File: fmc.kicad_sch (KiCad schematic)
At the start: 2 parts, among them P1 ASP-134604-01, P2 ASP-134604-01

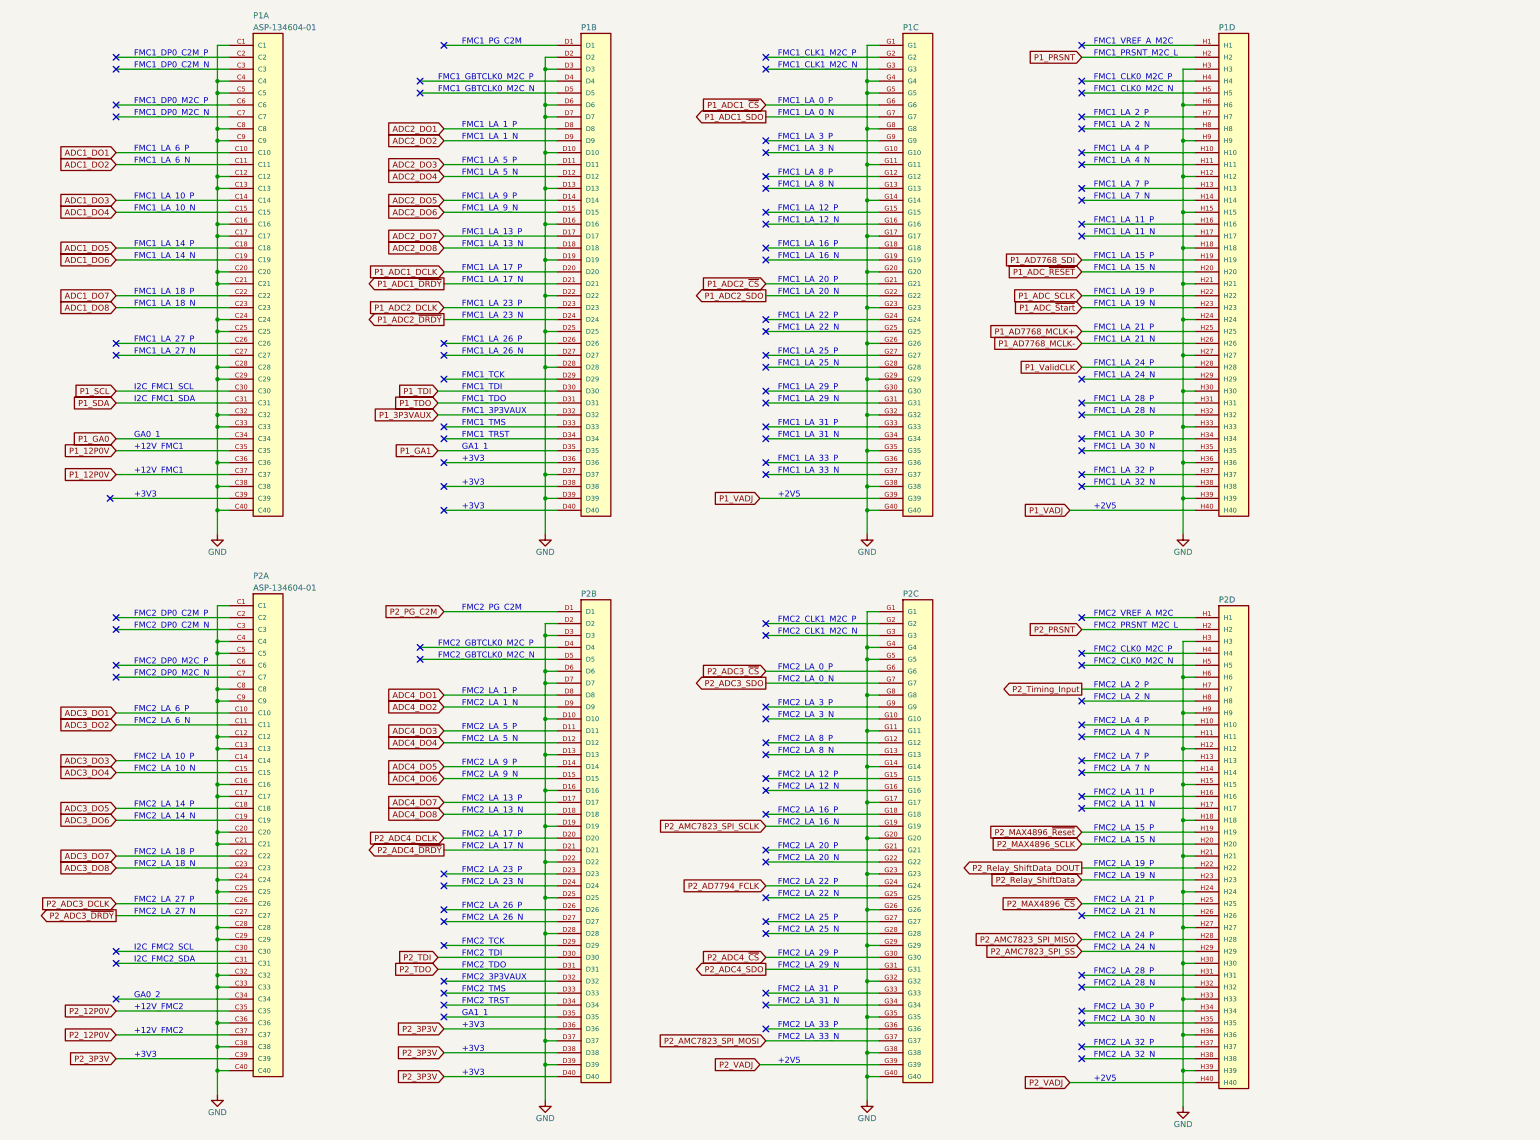
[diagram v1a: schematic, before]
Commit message: Update to Schematics; initial PCB commit
-Updated Power, Housekeeping, and ADCs sheets.
-Remapped FMC pins
-Initial board layout commit
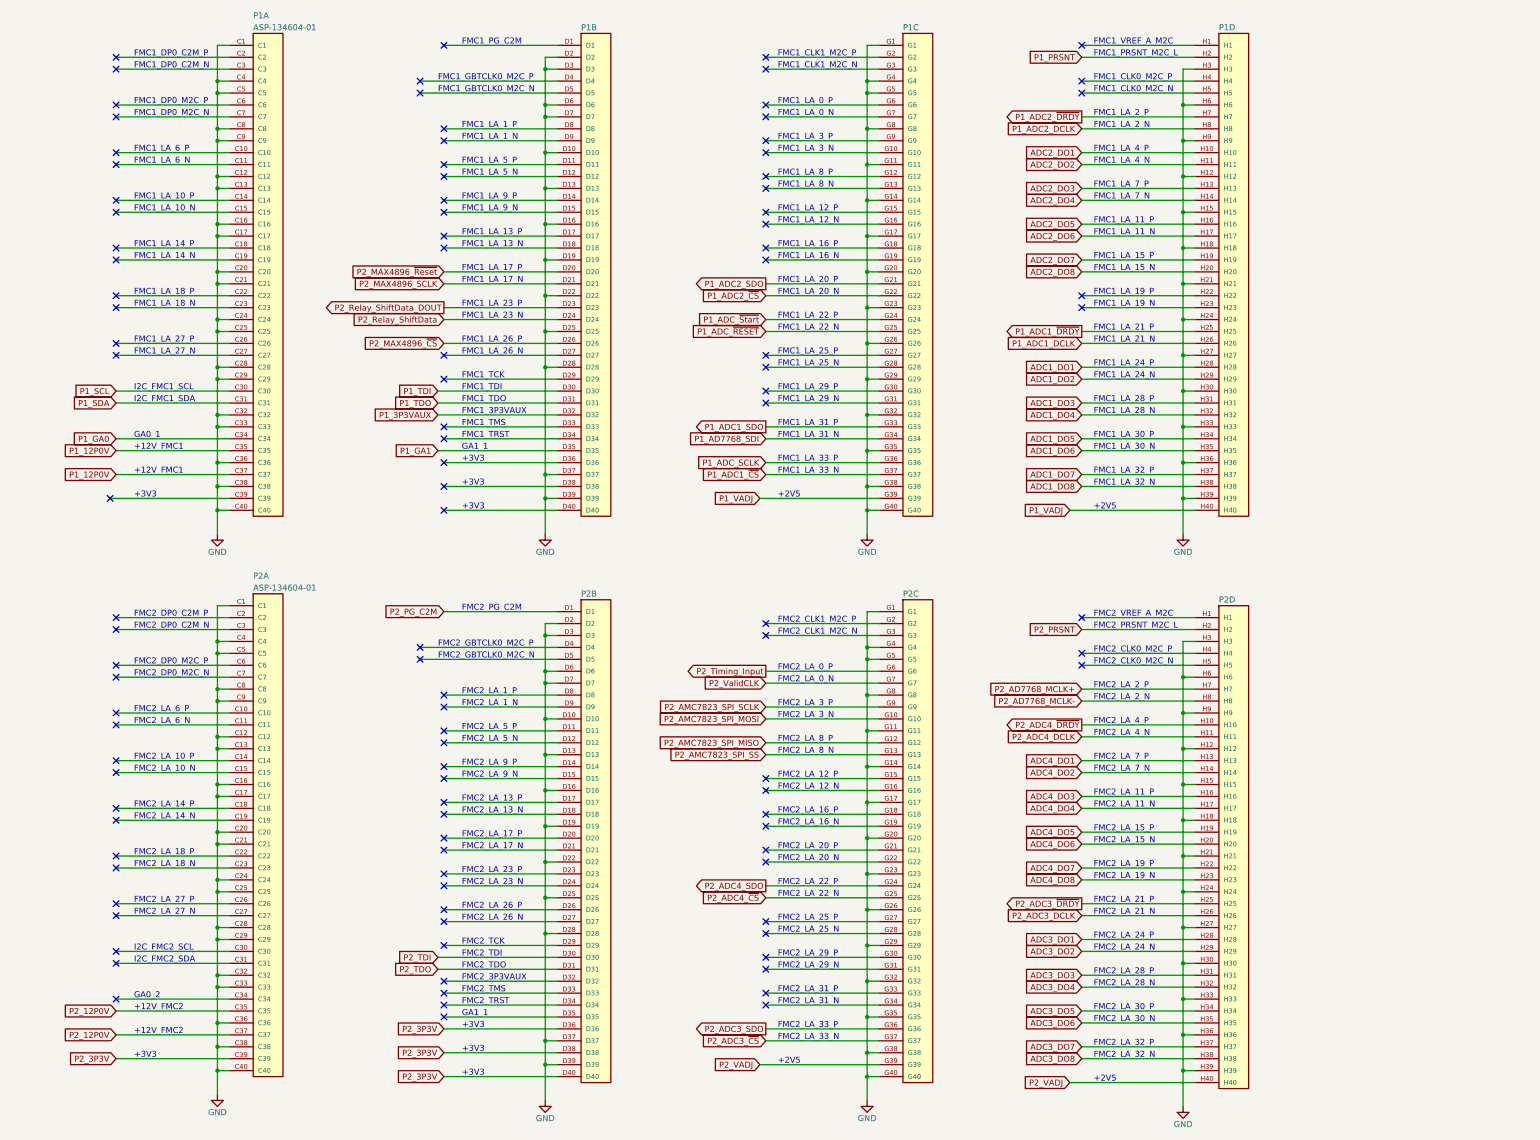
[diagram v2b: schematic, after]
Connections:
- net P1_AD7768_MCLK+ is gone; now on net P1_ADC1_~{DRDY}: P1.H25
- net P1_AD7768_MCLK- is gone; now on net P1_ADC1_DCLK: P1.H26
- net P1_ValidCLK is gone; now on net ADC1_DO1: P1.H28
- net P2_AD7794_FCLK is gone; now on net P2_ADC4_SDO: P2.G24
- net ADC1_DO1: no longer P1.C10
- net ADC1_DO2: now also P1.H29; no longer P1.C11
- net ADC1_DO3: now also P1.H31; no longer P1.C14
- net ADC1_DO4: now also P1.H32; no longer P1.C15
- net ADC1_DO5: now also P1.H34; no longer P1.C18
- net ADC1_DO6: now also P1.H35; no longer P1.C19
- net ADC1_DO7: now also P1.H37; no longer P1.C22
- net ADC1_DO8: now also P1.H38; no longer P1.C23
- net ADC2_DO1: now also P1.H10; no longer P1.D8
- net ADC2_DO2: now also P1.H11; no longer P1.D9
- net ADC2_DO3: now also P1.H13; no longer P1.D11
- net ADC2_DO4: now also P1.H14; no longer P1.D12
- net ADC2_DO5: now also P1.H16; no longer P1.D14
- net ADC2_DO6: now also P1.H17; no longer P1.D15
- net ADC2_DO7: now also P1.H19; no longer P1.D17
- net ADC2_DO8: now also P1.H20; no longer P1.D18
- net ADC3_DO1: now also P2.H28; no longer P2.C10
- net ADC3_DO2: now also P2.H29; no longer P2.C11
- net ADC3_DO3: now also P2.H31; no longer P2.C14
- net ADC3_DO4: now also P2.H32; no longer P2.C15
- net ADC3_DO5: now also P2.H34; no longer P2.C18
- net ADC3_DO6: now also P2.H35; no longer P2.C19
- net ADC3_DO7: now also P2.H37; no longer P2.C22
- net ADC3_DO8: now also P2.H38; no longer P2.C23
- net ADC4_DO1: now also P2.H13; no longer P2.D8
- net ADC4_DO2: now also P2.H14; no longer P2.D9
- net ADC4_DO3: now also P2.H16; no longer P2.D11
- net ADC4_DO4: now also P2.H17; no longer P2.D12
- net ADC4_DO5: now also P2.H19; no longer P2.D14
- net ADC4_DO6: now also P2.H20; no longer P2.D15
- net ADC4_DO7: now also P2.H22; no longer P2.D17
- net ADC4_DO8: now also P2.H23; no longer P2.D18
- net P1_AD7768_SDI: now also P1.G34; no longer P1.H19
- net P1_ADC1_DCLK: no longer P1.D20
- net P1_ADC1_SDO: now also P1.G33; no longer P1.G7
- net P1_ADC1_~{CS}: now also P1.G37; no longer P1.G6
- net P1_ADC1_~{DRDY}: no longer P1.D21
- net P1_ADC2_DCLK: now also P1.H8; no longer P1.D23
- net P1_ADC2_SDO: now also P1.G21; no longer P1.G22
- net P1_ADC2_~{CS}: now also P1.G22; no longer P1.G21
- net P1_ADC2_~{DRDY}: now also P1.H7; no longer P1.D24
- net P1_ADC_SCLK: now also P1.G36; no longer P1.H22
- net P1_ADC_~{RESET}: now also P1.G25; no longer P1.H20
- net P1_ADC_~{Start}: now also P1.G24; no longer P1.H23
- net P2_ADC3_DCLK: now also P2.H26; no longer P2.C26
- net P2_ADC3_SDO: now also P2.G36; no longer P2.G7
- net P2_ADC3_~{CS}: now also P2.G37; no longer P2.G6
- net P2_ADC3_~{DRDY}: now also P2.H25; no longer P2.C27
- net P2_ADC4_DCLK: now also P2.H11; no longer P2.D20
- net P2_ADC4_SDO: no longer P2.G31
- net P2_ADC4_~{CS}: now also P2.G25; no longer P2.G30
- net P2_ADC4_~{DRDY}: now also P2.H10; no longer P2.D21
- net P2_AMC7823_SPI_MISO: now also P2.G12; no longer P2.H28
- net P2_AMC7823_SPI_MOSI: now also P2.G10; no longer P2.G37
- net P2_AMC7823_SPI_SCLK: now also P2.G9; no longer P2.G19
- net P2_AMC7823_SPI_SS: now also P2.G13; no longer P2.H29
- net P2_MAX4896_SCLK: now also P1.D21; no longer P2.H20
- net P2_MAX4896_~{CS}: now also P1.D26; no longer P2.H25
- net P2_MAX4896_~{Reset}: now also P1.D20; no longer P2.H19
- net P2_Relay_ShiftData: now also P1.D24; no longer P2.H23
- net P2_Relay_ShiftData_DOUT: now also P1.D23; no longer P2.H22
- net P2_Timing_Input: now also P2.G6; no longer P2.H7
- net P2_AD7768_MCLK-: now reaches P2.H8
- new net P2_AD7768_MCLK+: P2.H7
- new net P2_ValidCLK: P2.G7
- no-connect marks 108 -> 109

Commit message: Updated Layout
-Additional Layout Work
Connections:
- net P1_ADC1_DCLK: now also P1.G33; no longer P1.H26
- net P1_ADC1_SDO: no longer P1.G33
- net P1_ADC1_~{DRDY}: no longer P1.H25
- net P1_ADC2_DCLK: now also P1.G27; no longer P1.H8
- net P1_ADC2_SDO: no longer P1.G21
- net P1_ADC2_~{CS}: now also P1.G28; no longer P1.G22
- net P1_ADC2_~{DRDY}: no longer P1.H7
- net P1_ADC_~{RESET}: now also P1.G31; no longer P1.G25
- net P1_ADC_~{Start}: now also P1.G30; no longer P1.G24
- net P2_MAX4896_~{Flag}: now reaches P2.D8
- no-connect marks 109 -> 104
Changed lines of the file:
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@@
   (no_connect (at 87.63 57.15))
   (no_connect (at 157.48 120.65))
-  (no_connect (at 157.48 160.02))
   (no_connect (at 226.06 147.32))
   (no_connect (at 87.63 34.29))
@@
   (no_connect (at 226.06 218.44))
   (no_connect (at 226.06 44.45))
-  (no_connect (at 226.06 87.63))
   (no_connect (at 226.06 67.31))
   (no_connect (at 293.37 74.93))
@@
   (no_connect (at 87.63 163.83))
   (no_connect (at 157.48 115.57))
-  (no_connect (at 226.06 95.25))
   (no_connect (at 157.48 64.77))
   (no_connect (at 157.48 162.56))
@@
   (no_connect (at 157.48 205.74))
   (no_connect (at 157.48 198.12))
-  (no_connect (at 226.06 90.17))
   (no_connect (at 157.48 223.52))
   (no_connect (at 157.48 105.41))
@@
   (no_connect (at 87.63 217.17))
   (no_connect (at 157.48 182.88))
-  (no_connect (at 226.06 97.79))
   (no_connect (at 157.48 208.28))
   (no_connect (at 226.06 215.9))
@@
     )
   )
-  (global_label "P1_ADC2_DCLK" (shape input) (at 293.37 39.37 180) (fields_autoplaced)
-    (effects (font (size 1.27 1.27)) (justify right))
-    (property "Intersheetrefs" "${INTERSHEET_REFS}" (at 276.2939 39.37 0)
-      (effects (font (size 1.27 1.27)) (justify right) hide)
-    )
-  )
   (global_label "P1_GA1" (shape input) (at 156.21 107.95 180) (fields_autoplaced)
     (effects (font (size 1.27 1.27)) (justify right))
@@
     )
   )
-  (global_label "P1_ADC2_SDO" (shape output) (at 226.06 72.39 180) (fields_autoplaced)
-    (effects (font (size 1.27 1.27)) (justify right))
-    (property "Intersheetrefs" "${INTERSHEET_REFS}" (at 210.012 72.39 0)
-      (effects (font (size 1.27 1.27)) (justify right) hide)
-    )
-  )
   (global_label "ADC3_DO6" (shape input) (at 293.37 229.87 180) (fields_autoplaced)
     (effects (font (size 1.27 1.27)) (justify right))
@@
     )
   )
+  (global_label "P1_ADC2_SDO" (shape output) (at 372.745 78.74 180) (fields_autoplaced)
+    (effects (font (size 1.27 1.27)) (justify right))
+    (property "Intersheetrefs" "${INTERSHEET_REFS}" (at 356.697 78.74 0)
+      (effects (font (size 1.27 1.27)) (justify right) hide)
+    )
+  )
   (global_label "ADC3_DO4" (shape input) (at 293.37 222.25 180) (fields_autoplaced)
     (effects (font (size 1.27 1.27)) (justify right))
@@
     )
   )
+  (global_label "P1_ADC2_~{CS}" (shape input) (at 226.06 90.17 180) (fields_autoplaced)
+    (effects (font (size 1.27 1.27)) (justify right))
+    (property "Intersheetrefs" "${INTERSHEET_REFS}" (at 211.3425 90.17 0)
+      (effects (font (size 1.27 1.27)) (justify right) hide)
+    )
+  )
   (global_label "ADC3_DO1" (shape input) (at 293.37 212.09 180) (fields_autoplaced)
     (effects (font (size 1.27 1.27)) (justify right))
@@
     )
   )
-  (global_label "P1_ADC2_~{CS}" (shape input) (at 226.06 74.93 180) (fields_autoplaced)
-    (effects (font (size 1.27 1.27)) (justify right))
-    (property "Intersheetrefs" "${INTERSHEET_REFS}" (at 211.3425 74.93 0)
-      (effects (font (size 1.27 1.27)) (justify right) hide)
-    )
-  )
   (global_label "P1_VADJ" (shape input) (at 224.79 118.11 180) (fields_autoplaced)
     (effects (font (size 1.27 1.27)) (justify right))
@@
     )
   )
+  (global_label "P2_MAX4896_~{Flag}" (shape input) (at 157.48 160.02 180) (fields_autoplaced)
+    (effects (font (size 1.27 1.27)) (justify right))
+    (property "Intersheetrefs" "${INTERSHEET_REFS}" (at 137.5202 160.02 0)
+      (effects (font (size 1.27 1.27)) (justify right) hide)
+    )
+  )
   (global_label "ADC4_DO1" (shape input) (at 293.37 173.99 180) (fields_autoplaced)
     (effects (font (size 1.27 1.27)) (justify right))
@@
     )
   )
-  (global_label "P1_ADC1_~{DRDY}" (shape output) (at 293.37 82.55 180) (fields_autoplaced)
-    (effects (font (size 1.27 1.27)) (justify right))
-    (property "Intersheetrefs" "${INTERSHEET_REFS}" (at 276.2334 82.55 0)
+  (global_label "P1_ADC1_DCLK" (shape input) (at 226.06 102.87 180) (fields_autoplaced)
+    (effects (font (size 1.27 1.27)) (justify right))
+    (property "Intersheetrefs" "${INTERSHEET_REFS}" (at 208.9839 102.87 0)
       (effects (font (size 1.27 1.27)) (justify right) hide)
     )
@@
     )
   )
+  (global_label "P1_ADC1_SDO" (shape output) (at 372.745 81.915 180) (fields_autoplaced)
+    (effects (font (size 1.27 1.27)) (justify right))
+    (property "Intersheetrefs" "${INTERSHEET_REFS}" (at 356.697 81.915 0)
+      (effects (font (size 1.27 1.27)) (justify right) hide)
+    )
+  )
   (global_label "P2_PG_C2M" (shape input) (at 157.48 142.24 180) (fields_autoplaced)
     (effects (font (size 1.27 1.27)) (justify right))
@@
     )
   )
+  (global_label "P1_ADC_~{Start}" (shape input) (at 226.06 95.25 180) (fields_autoplaced)
+    (effects (font (size 1.27 1.27)) (justify right))
+    (property "Intersheetrefs" "${INTERSHEET_REFS}" (at 210.4354 95.25 0)
+      (effects (font (size 1.27 1.27)) (justify right) hide)
+    )
+  )
   (global_label "ADC2_DO4" (shape input) (at 293.37 54.61 180) (fields_autoplaced)
     (effects (font (size 1.27 1.27)) (justify right))
@@
     )
   )
+  (global_label "P1_ADC2_~{DRDY}" (shape output) (at 354.965 78.74 180) (fields_autoplaced)
+    (effects (font (size 1.27 1.27)) (justify right))
+    (property "Intersheetrefs" "${INTERSHEET_REFS}" (at 337.8284 78.74 0)
+      (effects (font (size 1.27 1.27)) (justify right) hide)
+    )
+  )
   (global_label "ADC2_DO5" (shape input) (at 293.37 59.69 180) (fields_autoplaced)
     (effects (font (size 1.27 1.27)) (justify right))
@@
     )
   )
+  (global_label "P1_ADC2_DCLK" (shape input) (at 226.06 87.63 180) (fields_autoplaced)
+    (effects (font (size 1.27 1.27)) (justify right))
+    (property "Intersheetrefs" "${INTERSHEET_REFS}" (at 208.9839 87.63 0)
+      (effects (font (size 1.27 1.27)) (justify right) hide)
+    )
+  )
   (global_label "P2_ADC3_~{DRDY}" (shape output) (at 293.37 204.47 180) (fields_autoplaced)
     (effects (font (size 1.27 1.27)) (justify right))
@@
     )
   )
-  (global_label "P1_ADC1_DCLK" (shape input) (at 293.37 85.09 180) (fields_autoplaced)
-    (effects (font (size 1.27 1.27)) (justify right))
-    (property "Intersheetrefs" "${INTERSHEET_REFS}" (at 276.2939 85.09 0)
-      (effects (font (size 1.27 1.27)) (justify right) hide)
-    )
-  )
   (global_label "P2_3P3V" (shape input) (at 87.63 237.49 180) (fields_autoplaced)
     (effects (font (size 1.27 1.27)) (justify right))
@@
     )
   )
+  (global_label "P1_ADC_~{RESET}" (shape input) (at 226.06 97.79 180) (fields_autoplaced)
+    (effects (font (size 1.27 1.27)) (justify right))
+    (property "Intersheetrefs" "${INTERSHEET_REFS}" (at 209.2864 97.79 0)
+      (effects (font (size 1.27 1.27)) (justify right) hide)
+    )
+  )
   (global_label "P1_AD7768_SDI" (shape input) (at 226.06 105.41 180) (fields_autoplaced)
     (effects (font (size 1.27 1.27)) (justify right))
@@
     )
   )
-  (global_label "P1_ADC_~{RESET}" (shape input) (at 226.06 82.55 180) (fields_autoplaced)
-    (effects (font (size 1.27 1.27)) (justify right))
-    (property "Intersheetrefs" "${INTERSHEET_REFS}" (at 209.2864 82.55 0)
-      (effects (font (size 1.27 1.27)) (justify right) hide)
-    )
-  )
   (global_label "P2_PRSNT" (shape input) (at 293.37 146.05 180) (fields_autoplaced)
     (effects (font (size 1.27 1.27)) (justify right))
@@
     )
   )
-  (global_label "P1_ADC1_SDO" (shape output) (at 226.06 102.87 180) (fields_autoplaced)
-    (effects (font (size 1.27 1.27)) (justify right))
-    (property "Intersheetrefs" "${INTERSHEET_REFS}" (at 210.012 102.87 0)
-      (effects (font (size 1.27 1.27)) (justify right) hide)
-    )
-  )
   (global_label "P1_ADC_SCLK" (shape input) (at 226.06 110.49 180) (fields_autoplaced)
     (effects (font (size 1.27 1.27)) (justify right))
@@
     )
   )
-  (global_label "P1_ADC2_~{DRDY}" (shape output) (at 293.37 36.83 180) (fields_autoplaced)
-    (effects (font (size 1.27 1.27)) (justify right))
-    (property "Intersheetrefs" "${INTERSHEET_REFS}" (at 276.2334 36.83 0)
-      (effects (font (size 1.27 1.27)) (justify right) hide)
-    )
-  )
   (global_label "P2_Relay_ShiftData" (shape input) (at 157.48 80.01 180) (fields_autoplaced)
     (effects (font (size 1.27 1.27)) (justify right))
@@
     )
   )
-  (global_label "P1_ADC_~{Start}" (shape input) (at 226.06 80.01 180) (fields_autoplaced)
-    (effects (font (size 1.27 1.27)) (justify right))
-    (property "Intersheetrefs" "${INTERSHEET_REFS}" (at 210.4354 80.01 0)
-      (effects (font (size 1.27 1.27)) (justify right) hide)
-    )
-  )
   (global_label "ADC1_DO6" (shape input) (at 293.37 107.95 180) (fields_autoplaced)
     (effects (font (size 1.27 1.27)) (justify right))
@@
       (effects (font (size 1.27 1.27)) (justify right) hide)
     )
+  )
+  (global_label "P1_ADC1_~{DRDY}" (shape output) (at 354.965 81.915 180) (fields_autoplaced)
+    (effects (font (size 1.27 1.27)) (justify right))
+    (property "Intersheetrefs" "${INTERSHEET_REFS}" (at 337.8284 81.915 0)
+      (effects (font (size 1.27 1.27)) (justify right) hide)
+    )
